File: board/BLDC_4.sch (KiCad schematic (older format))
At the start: 21 parts, among them P1 Interface, P3 USB_B, P4 Power

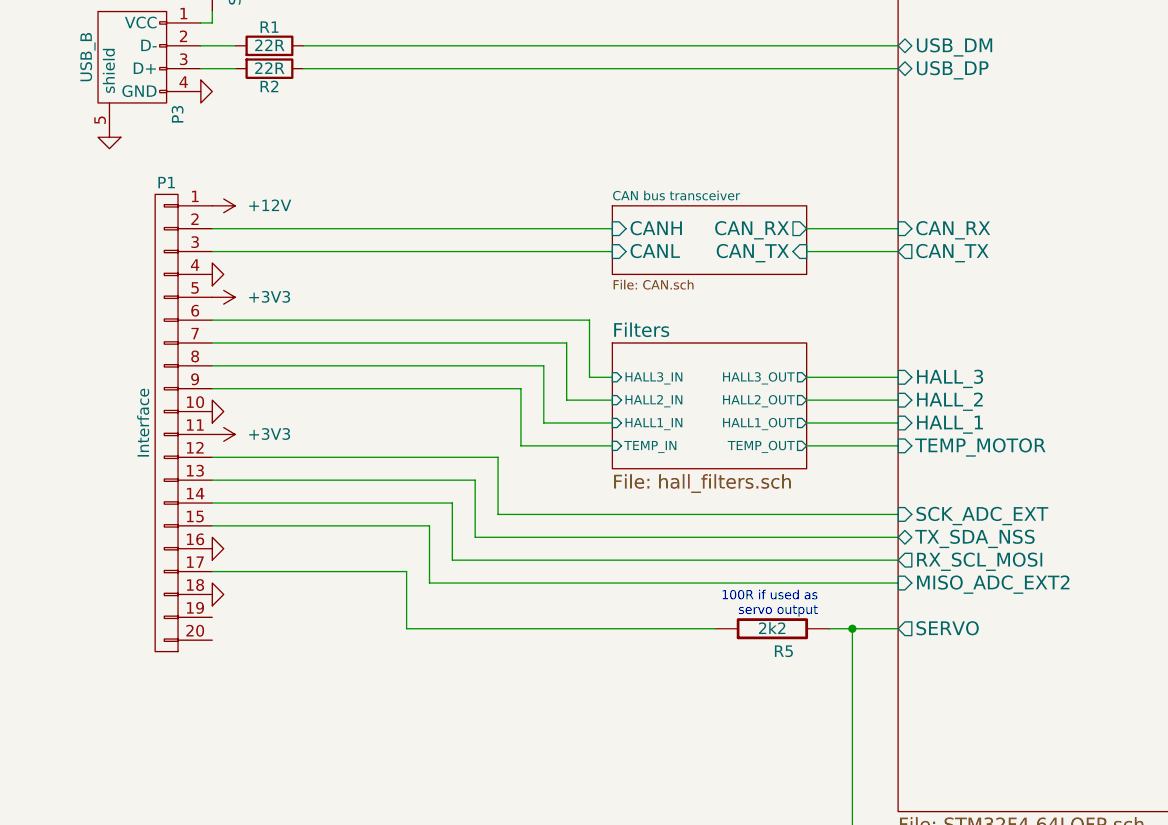
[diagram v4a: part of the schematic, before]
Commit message: - CAN interface isolation
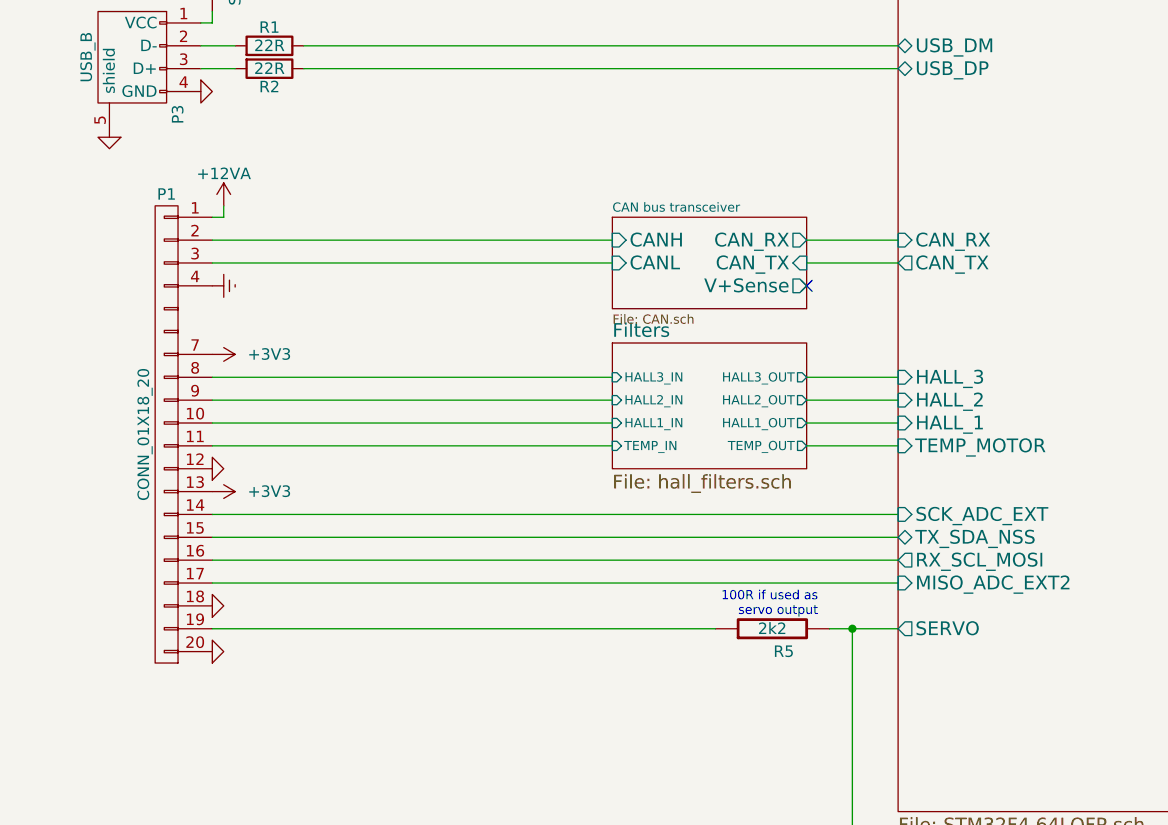
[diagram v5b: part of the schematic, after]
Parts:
- removed P1: Interface, alexmod:XG4A_20, symbol CONN_01X20
- added P1: CONN_01X18_20, alexmod:XG4A_20_wo_56, symbol CONN_01X18_20
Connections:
- net +3V3: now also P1.13 (P13), P1.7 (P7)
- net CAN bus transceiver/CANH: now also P1.2 (P2)
- net CAN bus transceiver/CANL: now also P1.3 (P3)
- net Filters/HALL1_IN: now also P1.10 (P10)
- net Filters/HALL2_IN: now also P1.9 (P9)
- net Filters/HALL3_IN: now also P1.8 (P8)
- net Filters/TEMP_IN: now also P1.11 (P11)
- net GND: now also P1.12 (P12), P1.18 (P18), P1.20 (P20)
- net MCU/MISO_ADC_EXT2: now also P1.17 (P17)
- net MCU/RX_SCL_MOSI: now also P1.16 (P16)
- net MCU/SCK_ADC_EXT: now also P1.14 (P14)
- net MCU/TX_SDA_NSS: now also P1.15 (P15)
- net at R5.1: now also P1.19 (P19)
- new net +12VA: P1.1 (P1)
- new net Earth: P1.4 (P4)
- no-connect marks 0 -> 1
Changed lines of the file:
@@
 Motorcontroler CPU
 $Sheet
-S 3750 3550 850  300
+S 3750 3600 850  400
 U 53FFB6E1
 F0 "CAN bus transceiver" 40
 F1 "CAN.sch" 40
-F2 "CAN_RX" O R 4600 3650 60
-F3 "CAN_TX" I R 4600 3750 60
-F4 "CANH" I L 3750 3650 60
-F5 "CANL" I L 3750 3750 60
+F2 "CAN_RX" O R 4600 3700 60
+F3 "CAN_TX" I R 4600 3800 60
+F4 "CANH" I L 3750 3700 60
+F5 "CANL" I L 3750 3800 60
+F6 "V+Sense" O R 4600 3900 60
 $EndSheet
 $Sheet
@@
 F20 "AN_IN" I R 7550 3600 60
 F21 "EN_GATE" O R 7550 2300 60
-F22 "CAN_RX" I L 5000 3650 60
-F23 "CAN_TX" O L 5000 3750 60
+F22 "CAN_RX" I L 5000 3700 60
+F23 "CAN_TX" O L 5000 3800 60
 F24 "LED_RED" O R 7550 5850 60
 F25 "LED_GREEN" O R 7550 5550 60
@@
 $EndComp
 $Comp
-L GND-RESCUE-BLDC_4 #PWR027
-U 1 1 57522C9D
-P 2000 3850
-F 0 "#PWR027" H 2000 3850 30  0001 C CNN
-F 1 "GND" H 2000 3780 30  0001 C CNN
-F 2 "" H 2000 3850 60  0001 C CNN
-F 3 "" H 2000 3850 60  0001 C CNN
-	1    2000 3850
-	0    -1   -1   0
-$EndComp
-$Comp
-L +3V3 #PWR028
+L +3V3 #PWR027
 U 1 1 57525DFB
-P 2000 3950
-F 0 "#PWR028" H 2000 3800 50  0001 C CNN
-F 1 "+3V3" V 2000 4200 50  0000 C CNN
-F 2 "" H 2000 3950 60  0000 C CNN
-F 3 "" H 2000 3950 60  0000 C CNN
-	1    2000 3950
+P 2000 4200
+F 0 "#PWR027" H 2000 4050 50  0001 C CNN
+F 1 "+3V3" V 2000 4450 50  0000 C CNN
+F 2 "" H 2000 4200 60  0000 C CNN
+F 3 "" H 2000 4200 60  0000 C CNN
+	1    2000 4200
 	0    1    1    0
 $EndComp
 $Comp
-L GND-RESCUE-BLDC_4 #PWR029
+L GND-RESCUE-BLDC_4 #PWR028
 U 1 1 575272EE
-P 2000 4450
-F 0 "#PWR029" H 2000 4450 30  0001 C CNN
-F 1 "GND" H 2000 4380 30  0001 C CNN
-F 2 "" H 2000 4450 60  0001 C CNN
-F 3 "" H 2000 4450 60  0001 C CNN
-	1    2000 4450
+P 2000 4700
+F 0 "#PWR028" H 2000 4700 30  0001 C CNN
+F 1 "GND" H 2000 4630 30  0001 C CNN
+F 2 "" H 2000 4700 60  0001 C CNN
+F 3 "" H 2000 4700 60  0001 C CNN
+	1    2000 4700
 	0    -1   -1   0
 $EndComp
 $Comp
-L CONN_01X20 P1
-U 1 1 57528DF6
-P 1800 4500
-F 0 "P1" H 1800 5550 50  0000 C CNN
-F 1 "Interface" V 1900 4500 50  0000 C CNN
-F 2 "alexmod:XG4A_20" H 1800 4500 60  0001 C CNN
-F 3 "" H 1800 4500 60  0000 C CNN
-	1    1800 4500
-	-1   0    0    -1
-$EndComp
-$Comp
-L GND-RESCUE-BLDC_4 #PWR030
+L GND-RESCUE-BLDC_4 #PWR029
 U 1 1 5752E9ED
-P 2000 5050
-F 0 "#PWR030" H 2000 5050 30  0001 C CNN
-F 1 "GND" H 2000 4980 30  0001 C CNN
-F 2 "" H 2000 5050 60  0001 C CNN
-F 3 "" H 2000 5050 60  0001 C CNN
-	1    2000 5050
+P 2000 5300
+F 0 "#PWR029" H 2000 5300 30  0001 C CNN
+F 1 "GND" H 2000 5230 30  0001 C CNN
+F 2 "" H 2000 5300 60  0001 C CNN
+F 3 "" H 2000 5300 60  0001 C CNN
+	1    2000 5300
 	0    -1   -1   0
 $EndComp
 $Comp
-L +3V3 #PWR031
+L +3V3 #PWR030
 U 1 1 5752F2C9
-P 2000 4550
-F 0 "#PWR031" H 2000 4400 50  0001 C CNN
-F 1 "+3V3" V 2000 4800 50  0000 C CNN
-F 2 "" H 2000 4550 60  0000 C CNN
-F 3 "" H 2000 4550 60  0000 C CNN
-	1    2000 4550
+P 2000 4800
+F 0 "#PWR030" H 2000 4650 50  0001 C CNN
+F 1 "+3V3" V 2000 5050 50  0000 C CNN
+F 2 "" H 2000 4800 60  0000 C CNN
+F 3 "" H 2000 4800 60  0000 C CNN
+	1    2000 4800
 	0    1    1    0
 $EndComp
 $Comp
-L GND-RESCUE-BLDC_4 #PWR032
+L GND-RESCUE-BLDC_4 #PWR031
 U 1 1 57536FDB
-P 2000 5250
-F 0 "#PWR032" H 2000 5250 30  0001 C CNN
-F 1 "GND" H 2000 5180 30  0001 C CNN
-F 2 "" H 2000 5250 60  0001 C CNN
-F 3 "" H 2000 5250 60  0001 C CNN
-	1    2000 5250
+P 2000 5500
+F 0 "#PWR031" H 2000 5500 30  0001 C CNN
+F 1 "GND" H 2000 5430 30  0001 C CNN
+F 2 "" H 2000 5500 60  0001 C CNN
+F 3 "" H 2000 5500 60  0001 C CNN
+	1    2000 5500
 	0    -1   -1   0
 $EndComp
 $Comp
-L +3V3 #PWR033
+L +3V3 #PWR032
 U 1 1 575425B1
 P 8050 5250
-F 0 "#PWR033" H 8050 5100 50  0001 C CNN
+F 0 "#PWR032" H 8050 5100 50  0001 C CNN
 F 1 "+3V3" H 8050 5390 50  0000 C CNN
 F 2 "" H 8050 5250 60  0000 C CNN
@@
 $EndComp
 $Comp
-L GND-RESCUE-BLDC_4 #PWR034
+L GND-RESCUE-BLDC_4 #PWR033
 U 1 1 5755CD59
 P 1950 3050
-F 0 "#PWR034" H 1950 3050 30  0001 C CNN
+F 0 "#PWR033" H 1950 3050 30  0001 C CNN
 F 1 "GND" H 1950 2980 30  0001 C CNN
 F 2 "" H 1950 3050 60  0001 C CNN
@@
 $EndComp
 $Comp
-L GND-RESCUE-BLDC_4 #PWR035
+L GND-RESCUE-BLDC_4 #PWR034
 U 1 1 5755CE93
 P 1550 3250
-F 0 "#PWR035" H 1550 3250 30  0001 C CNN
+F 0 "#PWR034" H 1550 3250 30  0001 C CNN
 F 1 "GND" H 1550 3180 30  0001 C CNN
 F 2 "" H 1550 3250 60  0001 C CNN
@@
 	5000 4600 4600 4600
 Wire Wire Line
-	4600 3650 5000 3650
+	4600 3700 5000 3700
 Wire Wire Line
-	5000 3750 4600 3750
+	5000 3800 4600 3800
 Wire Wire Line
 	1950 2850 2100 2850
@@
 	7550 3500 9900 3500
 Wire Wire Line
-	3750 3750 2000 3750
-Wire Wire Line
-	2000 3650 3750 3650
-Wire Wire Line
-	2000 4050 3650 4050
-Wire Wire Line
-	3650 4050 3650 4300
-Wire Wire Line
-	3650 4300 3750 4300
-Wire Wire Line
-	2000 4150 3550 4150
-Wire Wire Line
-	3550 4150 3550 4400
-Wire Wire Line
-	3550 4400 3750 4400
-Wire Wire Line
-	2000 4250 3450 4250
-Wire Wire Line
-	3450 4250 3450 4500
-Wire Wire Line
-	3450 4500 3750 4500
-Wire Wire Line
-	2000 4350 3350 4350
-Wire Wire Line
-	3350 4350 3350 4600
-Wire Wire Line
-	3350 4600 3750 4600
-Wire Wire Line
-	3250 4650 3250 4900
-Wire Wire Line
-	3250 4900 5000 4900
-Wire Wire Line
-	3150 4750 3150 5000
-Wire Wire Line
-	3150 5000 5000 5000
-Wire Wire Line
-	5000 5100 3050 5100
+	3750 3800 2000 3800
 Wire Wire Line
-	3050 5100 3050 4850
+	2000 3700 3750 3700
 Wire Wire Line
-	2950 4950 2950 5200
+	2000 4400 3750 4400
 Wire Wire Line
-	2950 5200 5000 5200
+	2000 4500 3750 4500
 Wire Wire Line
-	2950 4950 2000 4950
+	2000 4600 3750 4600
 Wire Wire Line
-	3250 4650 2000 4650
+	2000 4900 5000 4900
 Wire Wire Line
-	2000 4750 3150 4750
+	2000 5000 5000 5000
 Wire Wire Line
-	3050 4850 2000 4850
+	2000 5100 5000 5100
 Wire Wire Line
-	4200 5400 2850 5400
+	2000 5200 5000 5200
 Wire Wire Line
-	2850 5400 2850 5150
-Wire Wire Line
-	2850 5150 2000 5150
+	2000 5400 4200 5400
 Wire Wire Line
 	7550 5850 8050 5850
@@
 $EndComp
 $Comp
-L GND-RESCUE-BLDC_4 #PWR036
+L GND-RESCUE-BLDC_4 #PWR035
 U 1 1 5757A76E
 P 7750 4550
-F 0 "#PWR036" H 7750 4550 30  0001 C CNN
+F 0 "#PWR035" H 7750 4550 30  0001 C CNN
 F 1 "GND" H 7750 4480 30  0001 C CNN
 F 2 "" H 7750 4550 60  0001 C CNN
@@
 $EndComp
 $Comp
-L GND-RESCUE-BLDC_4 #PWR037
+L GND-RESCUE-BLDC_4 #PWR036
 U 1 1 5757B5DF
 P 7950 4550
-F 0 "#PWR037" H 7950 4550 30  0001 C CNN
+F 0 "#PWR036" H 7950 4550 30  0001 C CNN
 F 1 "GND" H 7950 4480 30  0001 C CNN
 F 2 "" H 7950 4550 60  0001 C CNN
@@
 $EndComp
 $Comp
-L GND-RESCUE-BLDC_4 #PWR038
+L GND-RESCUE-BLDC_4 #PWR037
 U 1 1 5757B722
 P 8150 4550
-F 0 "#PWR038" H 8150 4550 30  0001 C CNN
+F 0 "#PWR037" H 8150 4550 30  0001 C CNN
 F 1 "GND" H 8150 4480 30  0001 C CNN
 F 2 "" H 8150 4550 60  0001 C CNN
@@
 $EndComp
 $Comp
-L GND-RESCUE-BLDC_4 #PWR039
+L GND-RESCUE-BLDC_4 #PWR038
 U 1 1 5757C875
 P 8350 4550
-F 0 "#PWR039" H 8350 4550 30  0001 C CNN
+F 0 "#PWR038" H 8350 4550 30  0001 C CNN
 F 1 "GND" H 8350 4480 30  0001 C CNN
 F 2 "" H 8350 4550 60  0001 C CNN
@@
 $EndComp
 $Comp
-L GND-RESCUE-BLDC_4 #PWR040
+L GND-RESCUE-BLDC_4 #PWR039
 U 1 1 5757FA73
 P 8550 4550
-F 0 "#PWR040" H 8550 4550 30  0001 C CNN
+F 0 "#PWR039" H 8550 4550 30  0001 C CNN
 F 1 "GND" H 8550 4480 30  0001 C CNN
 F 2 "" H 8550 4550 60  0001 C CNN
@@
 $EndComp
 $Comp
-L GND-RESCUE-BLDC_4 #PWR041
+L GND-RESCUE-BLDC_4 #PWR040
 U 1 1 5757FA7F
 P 8750 4550
-F 0 "#PWR041" H 8750 4550 30  0001 C CNN
+F 0 "#PWR040" H 8750 4550 30  0001 C CNN
 F 1 "GND" H 8750 4480 30  0001 C CNN
 F 2 "" H 8750 4550 60  0001 C CNN
@@
 $EndComp
 $Comp
-L GND-RESCUE-BLDC_4 #PWR042
+L GND-RESCUE-BLDC_4 #PWR041
 U 1 1 5757FA8B
 P 8950 4550
-F 0 "#PWR042" H 8950 4550 30  0001 C CNN
+F 0 "#PWR041" H 8950 4550 30  0001 C CNN
 F 1 "GND" H 8950 4480 30  0001 C CNN
 F 2 "" H 8950 4550 60  0001 C CNN
@@
 	8950 4250 8950 3000
 Connection ~ 8950 3000
-$Comp
-L +12V #PWR043
-U 1 1 57574636
-P 2000 3550
-F 0 "#PWR043" H 2000 3400 50  0001 C CNN
-F 1 "+12V" V 2000 3800 50  0000 C CNN
-F 2 "" H 2000 3550 50  0000 C CNN
-F 3 "" H 2000 3550 50  0000 C CNN
-	1    2000 3550
-	0    1    1    0
-$EndComp
 $Sheet
 S 9300 900  1100 550
@@
 $EndComp
 $Comp
-L +5V #PWR044
+L +5V #PWR042
 U 1 1 575812F1
 P 2000 2500
-F 0 "#PWR044" H 2000 2350 50  0001 C CNN
+F 0 "#PWR042" H 2000 2350 50  0001 C CNN
 F 1 "+5V" H 2000 2640 50  0000 C CNN
 F 2 "" H 2000 2500 60  0000 C CNN
@@
 	2000 2750 1950 2750
 $Comp
-L +5V #PWR045
+L +5V #PWR043
 U 1 1 5758912C
 P 9900 4100
-F 0 "#PWR045" H 9900 3950 50  0001 C CNN
+F 0 "#PWR043" H 9900 3950 50  0001 C CNN
 F 1 "+5V" V 9900 4350 50  0000 C CNN
 F 2 "" H 9900 4100 60  0000 C CNN
@@
 	0    -1   -1   0
 $EndComp
+$Comp
+L +12VA #PWR044
+U 1 1 575987D7
+P 2050 3550
+F 0 "#PWR044" H 2050 3400 50  0001 C CNN
+F 1 "+12VA" H 2050 3690 50  0000 C CNN
+F 2 "" H 2050 3550 60  0000 C CNN
+F 3 "" H 2050 3550 60  0000 C CNN
+	1    2050 3550
+	1    0    0    -1
+$EndComp
+Wire Wire Line
+	2050 3550 2050 3600
+Wire Wire Line
+	2050 3600 2000 3600
+NoConn ~ 4600 3900
+$Comp
+L Earth #PWR045
+U 1 1 575A52B4
+P 2000 3900
+F 0 "#PWR045" H 2000 3650 50  0001 C CNN
+F 1 "Earth" H 2000 3750 50  0001 C CNN
+F 2 "" H 2000 3900 60  0000 C CNN
+F 3 "" H 2000 3900 60  0000 C CNN
+	1    2000 3900
+	0    -1   -1   0
+$EndComp
+Wire Wire Line
+	3750 4300 2000 4300
+$Comp
+L CONN_01X18_20 P1
+U 1 1 575BB9C3
+P 1800 4550
+F 0 "P1" H 1800 5600 50  0000 C CNN
+F 1 "CONN_01X18_20" V 1900 4550 50  0000 C CNN
+F 2 "alexmod:XG4A_20_wo_56" H 1800 4550 60  0001 C CNN
+F 3 "" H 1800 4550 60  0000 C CNN
+	1    1800 4550
+	-1   0    0    -1
+$EndComp
 $EndSCHEMATC
